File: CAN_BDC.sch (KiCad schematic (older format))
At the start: 26 parts, among them P1 CONN_01X05, P2 CONN_01X02, P4 CONN_01X02, P5 CONN_01X02, P6 CONN_01X02, U1 STM32F042C6Ux, U2 PSD2CAN, U3 SN65HVD232D, U5 MCP1700T-3302E/TT

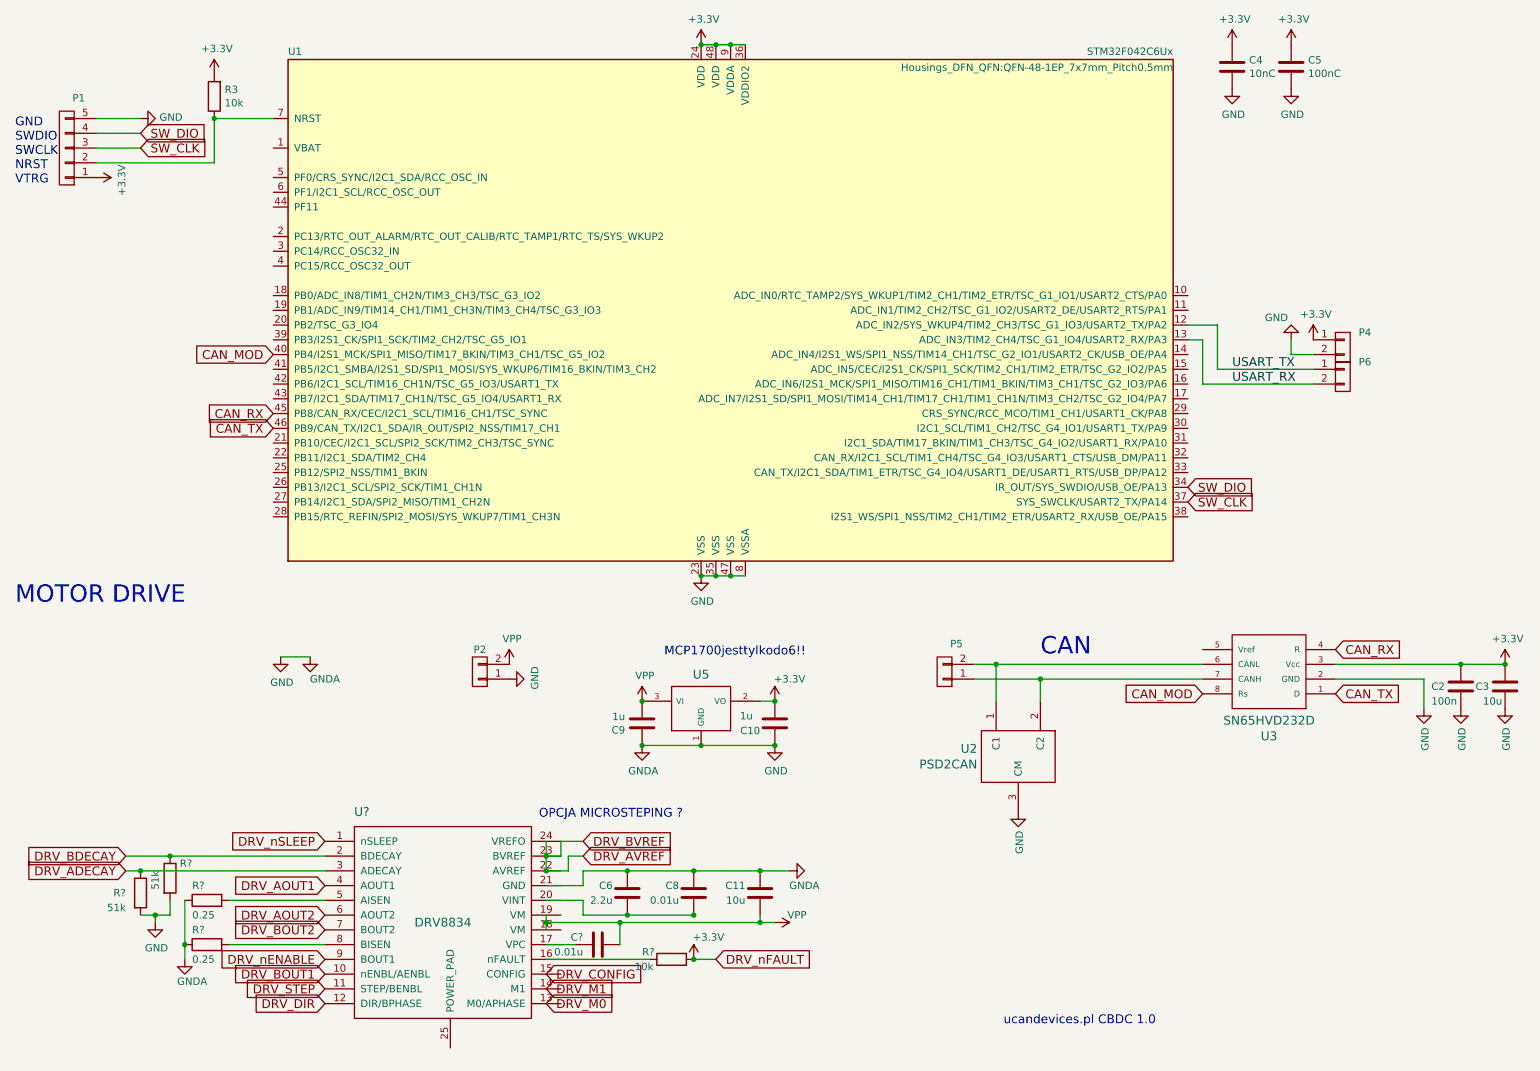
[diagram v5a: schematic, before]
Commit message: DRV8834 board update
DRV8834 board update
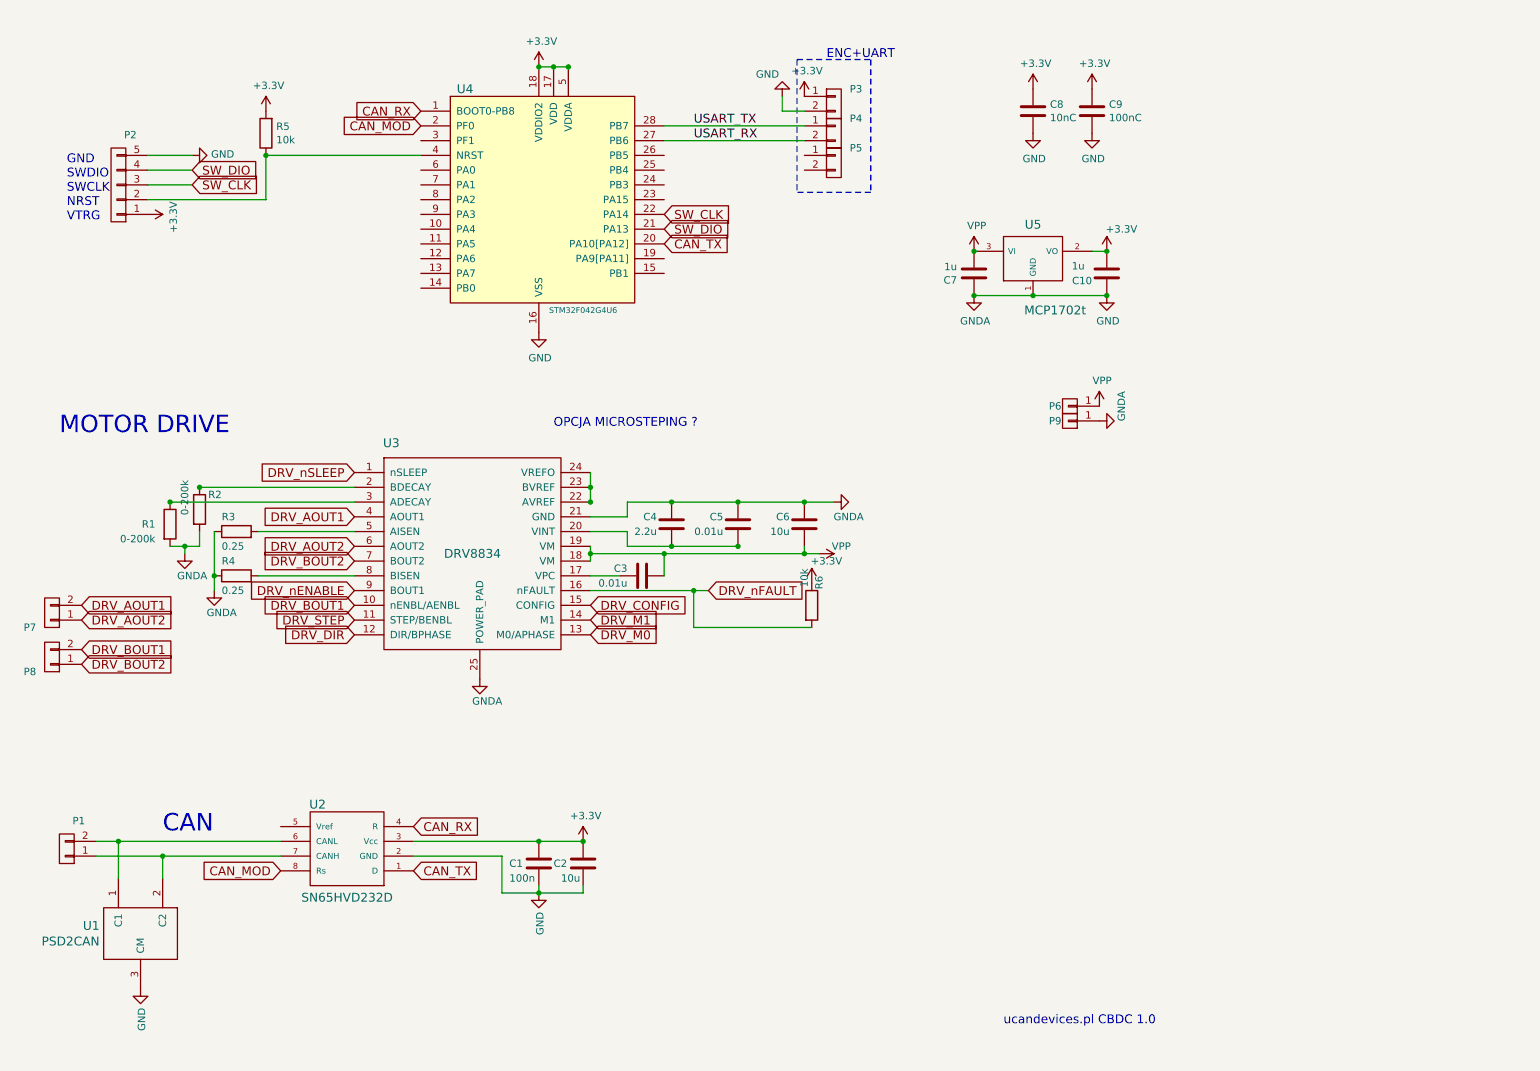
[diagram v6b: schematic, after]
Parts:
- removed P2: CONN_01X02, Pin_Headers:Pin_Header_Straight_1x02, symbol CONN_01X02
- removed U1: STM32F042C6Ux, Housings_DFN_QFN:QFN-48-1EP_7x7mm_Pitch0.5mm, symbol STM32F042C6Ux
- added P5, P7, P8: CONN_01X02, Pin_Headers:Pin_Header_Straight_1x02_Pitch2.00mm, symbol CONN_01X02
- added P6, P9: CONN_01X01, Pin_Headers:Pin_Header_Straight_1x01, symbol CONN_01X01
- added U4: STM32F042G4U6, usb_ccb_custom:UFQFPN_28, symbol STM32F042C6T6
- P1: renamed from P5; footprint Pin_Headers:Pin_Header_Straight_1x02 -> Pin_Headers:Pin_Header_Straight_1x02_Pitch2.00mm
- P3: renamed from P4; footprint Pin_Headers:Pin_Header_Straight_1x02 -> Pin_Headers:Pin_Header_Straight_1x02_Pitch2.00mm
- P4: renamed from P6; footprint Pin_Headers:Pin_Header_Straight_1x02 -> Pin_Headers:Pin_Header_Straight_1x02_Pitch2.00mm
- R1, R2: renamed from R?; value 51k -> 0-200k
- U5: value MCP1700T-3302E/TT -> MCP1702t
- gave numbers to parts that had none: 5
- renumbered C2 to C1, C3 to C2, C6 to C4, C8 to C5, C11 to C6, C9 to C7, C4 to C8, C5 to C9, P1 to P2, R3 to R5, U2 to U1, U3 to U2
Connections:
- net labels removed: DRV_ADECAY, DRV_AVREF, DRV_BDECAY, DRV_BVREF
- wire segments 54 -> 46
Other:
- note added: "ENC+UART"
- note removed: "MCP1700jesttylkodo6!!"
- moved on the sheet: C1, C10, C2, C3, C4, C5, C6, C7, C8, C9, P1, P2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

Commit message: Pcb wirring 1
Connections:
- net DRV_BOUT1: now also U3.9 (BOUT1); no longer U3.10 (nENBL/AENBL)
- net DRV_CONFIG: now also U4.7 (PA1)
- net DRV_M0: now also U4.9 (PA3)
- net DRV_M1: now also U4.8 (PA2)
- net DRV_nENABLE: now also U3.10 (nENBL/AENBL); no longer U3.9 (BOUT1)
- net DRV_nFAULT: now also U4.6 (PA0)
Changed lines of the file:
@@
 Text GLabel 3000 3750 0    60   Input ~ 0
 DRV_nSLEEP
-Text GLabel 3000 4650 0    60   Input ~ 0
+Text GLabel 3000 4550 0    60   Input ~ 0
 DRV_BOUT1
 Text GLabel 3000 4750 0    60   Input ~ 0
@@
 	1    0    0    -1
 $EndComp
-Text GLabel 3000 4550 0    60   Input ~ 0
+Text GLabel 3000 4650 0    60   Input ~ 0
 DRV_nENABLE
 Text GLabel 3000 4350 0    60   Input ~ 0
@@
 	1    0    0    -1
 $EndComp
+Text GLabel 3450 1700 0    60   Input ~ 0
+DRV_nFAULT
+Text GLabel 3450 1800 0    60   Input ~ 0
+DRV_CONFIG
+Text GLabel 3450 1900 0    60   Input ~ 0
+DRV_M1
+Text GLabel 3450 2000 0    60   Input ~ 0
+DRV_M0
 $EndSCHEMATC

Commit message: Tracks Placement Motor
Tracks Placement Motor
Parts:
- removed R1, R2: 0-200k, Resistors_SMD:R_0402, symbol R
- R3, R4: footprint Resistors_SMD:R_0402 -> Resistors_SMD:R_2512
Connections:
- net DRV_BDECAY: now reaches U3.2 (BDECAY)
- net DRV_ADECAY: now reaches U3.3 (ADECAY)
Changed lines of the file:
@@
 F 0 "R3" V 2300 4250 50  0000 R CNN
 F 1 "0.25" V 2100 4250 50  0000 R CNN
-F 2 "Resistors_SMD:R_0402" H 2130 4241 50  0001 R CNN
+F 2 "Resistors_SMD:R_2512" H 2130 4241 50  0001 R CNN
 F 3 "" H 2200 4150 50  0000 C CNN
 	1    2200 4150
@@
 F 0 "R4" V 2300 4550 50  0000 R CNN
 F 1 "0.25" V 2100 4550 50  0000 R CNN
-F 2 "Resistors_SMD:R_0402" H 2130 4541 50  0001 R CNN
+F 2 "Resistors_SMD:R_2512" H 2130 4541 50  0001 R CNN
 F 3 "" H 2200 4450 50  0000 C CNN
 	1    2200 4450
@@
 	5100 4450 5100 4300
 Connection ~ 5100 4300
-$Comp
-L R R1
-U 1 1 58035F1A
-P 1750 4100
-F 0 "R1" H 1650 4100 50  0000 R CNN
-F 1 "0-200k" H 1650 4000 50  0000 R CNN
-F 2 "Resistors_SMD:R_0402" H 1680 4191 50  0001 R CNN
-F 3 "" H 1750 4100 50  0000 C CNN
-	1    1750 4100
-	1    0    0    -1
-$EndComp
-$Comp
-L R R2
-U 1 1 58036074
-P 1950 4000
-F 0 "R2" H 2100 4100 50  0000 R CNN
-F 1 "0-200k" V 1850 4200 50  0000 R CNN
-F 2 "Resistors_SMD:R_0402" H 1880 4091 50  0001 R CNN
-F 3 "" H 1950 4000 50  0000 C CNN
-	1    1950 4000
-	1    0    0    -1
-$EndComp
-Wire Wire Line
-	1950 4150 1950 4250
-Wire Wire Line
-	1950 4250 1750 4250
-Wire Wire Line
-	1850 4250 1850 4300
-Connection ~ 1850 4250
 Wire Wire Line
 	4600 3750 4600 3950
@@
 Text GLabel 1150 4950 2    60   Input ~ 0
 DRV_BOUT1
-Wire Wire Line
-	1750 3950 3000 3950
-Wire Wire Line
-	3000 3850 1950 3850
-Connection ~ 1750 3950
-Connection ~ 1950 3850
 $Comp
 L CONN_01X01 P6
@@
 	-1   0    0    1
 $EndComp
-$Comp
-L GNDA #PWR026
-U 1 1 580704FB
-P 1850 4300
-F 0 "#PWR026" H 1850 4050 50  0001 C CNN
-F 1 "GNDA" H 1900 4150 50  0000 C CNN
-F 2 "" H 1850 4300 50  0000 C CNN
-F 3 "" H 1850 4300 50  0000 C CNN
-	1    1850 4300
-	1    0    0    -1
-$EndComp
 Text GLabel 3450 1700 0    60   Input ~ 0
 DRV_nFAULT
@@
 Text GLabel 3450 2000 0    60   Input ~ 0
 DRV_M0
+Text GLabel 3000 3850 0    60   Input ~ 0
+DRV_BDECAY
+Text GLabel 3000 3950 0    60   Input ~ 0
+DRV_ADECAY
+Text GLabel 3200 2600 0    60   Input ~ 0
+DRV_ADECAY
+Text GLabel 3200 2500 0    60   Input ~ 0
+DRV_BDECAY
+Text GLabel 2150 2400 0    60   Input ~ 0
+DRV_nENABLE
+Text GLabel 2150 2500 0    60   Input ~ 0
+DRV_STEP
+Text GLabel 2150 2600 0    60   Input ~ 0
+DRV_DIR
 $EndSCHEMATC
